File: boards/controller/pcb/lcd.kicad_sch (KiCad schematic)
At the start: 9 parts, among them J1001 Conn_01x15_Socket

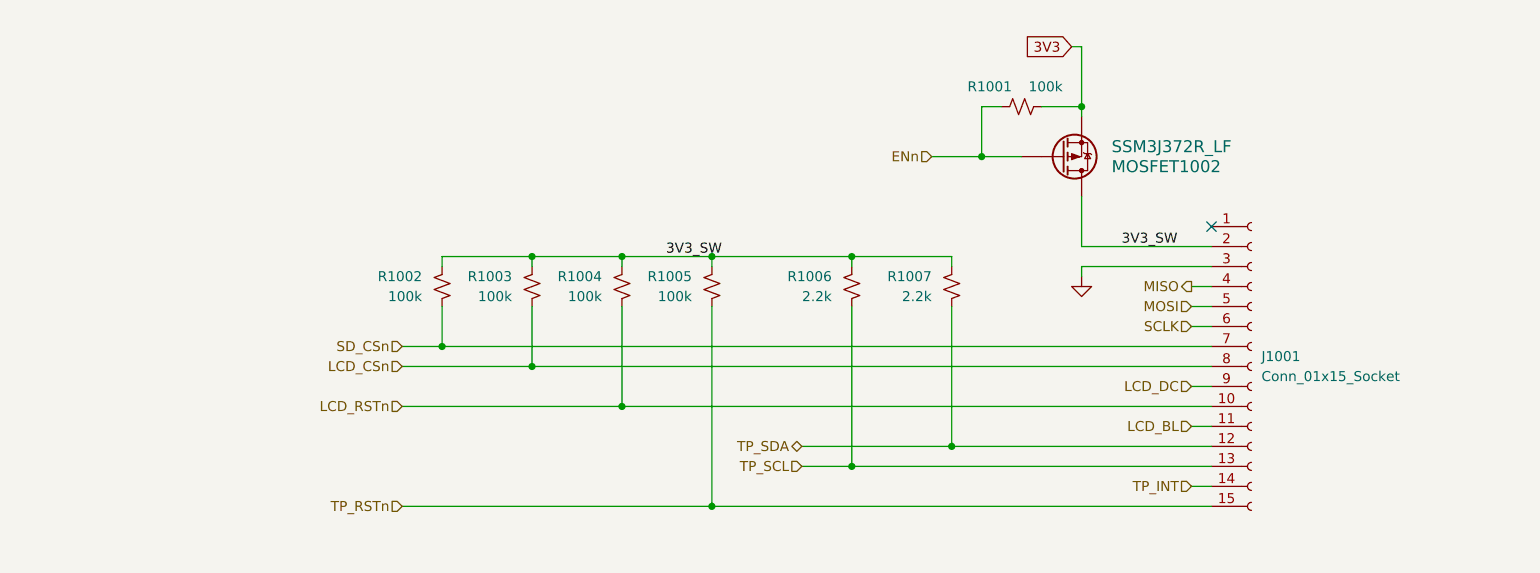
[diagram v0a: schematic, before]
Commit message: controller: pcb: Update schematic
Signed-off-by: Nicholas Loehrke <nicholasnloehrke@gmail.com>
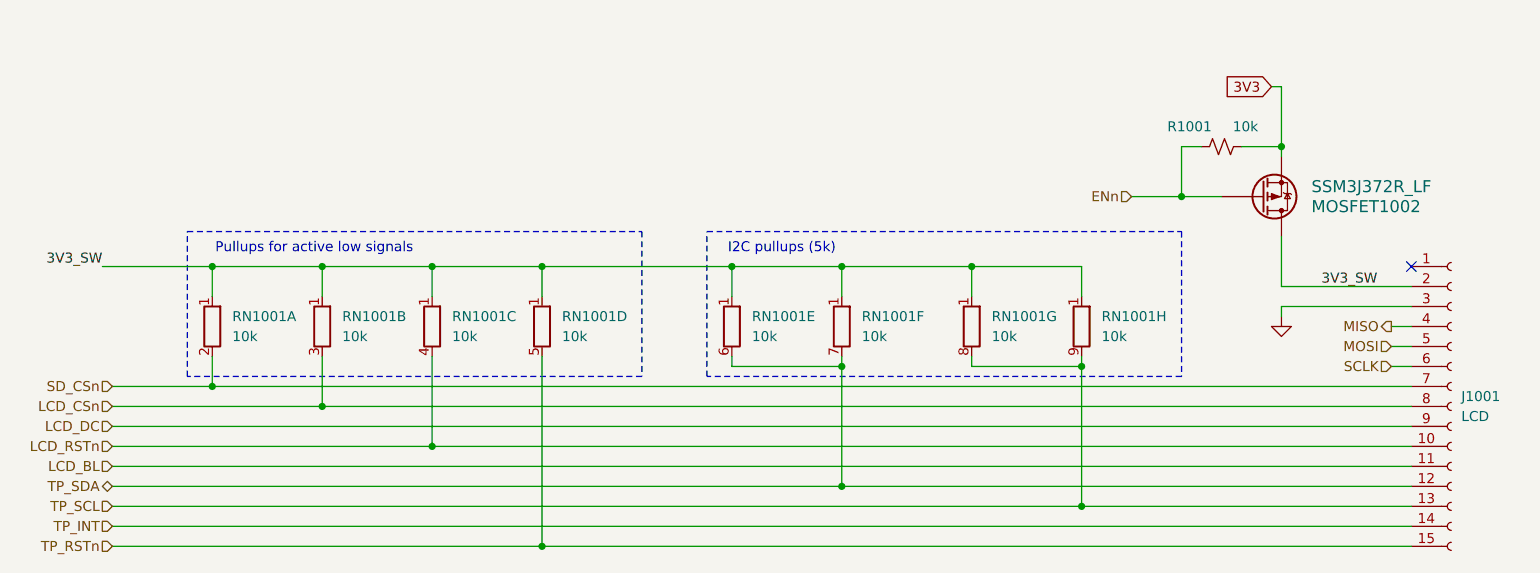
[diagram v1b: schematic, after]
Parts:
- removed R1002, R1003, R1004, R1005: 100k, symbol Device:R_Small_US
- removed R1006, R1007: 2.2k, symbol Device:R_Small_US
- added RN1001: 10k, Resistor_THT:R_Array_SIP9, symbol Device:R_Network08_Split
- J1001: value Conn_01x15_Socket -> LCD
- R1001: value 100k -> 10k
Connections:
- net 3V3_SW: now also RN1001.1 (R1), RN1001.1 (R1), RN1001.1 (R1), RN1001.1 (R1), RN1001.1 (R1), RN1001.1 (R1), RN1001.1 (R1), RN1001.1 (R1)
- net LCD_CSn: now also RN1001.3 (R2.2)
- net LCD_RSTn: now also RN1001.4 (R3.2)
- net SD_CSn: now also RN1001.2 (R1.2)
- net TP_RSTn: now also RN1001.5 (R4.2)
- net TP_SCL: now also RN1001.8 (R7.2), RN1001.9 (R8.2)
- net TP_SDA: now also RN1001.6 (R5.2), RN1001.7 (R6.2)
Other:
- note added: "I2C pullups (5k)"
- note added: "Pullups for active low signals"
- moved on the sheet: J1001, MOSFET1002, R1001

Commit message: controller: pcb: Update schematic
Signed-off-by: Nicholas Loehrke <nicholasnloehrke@gmail.com>
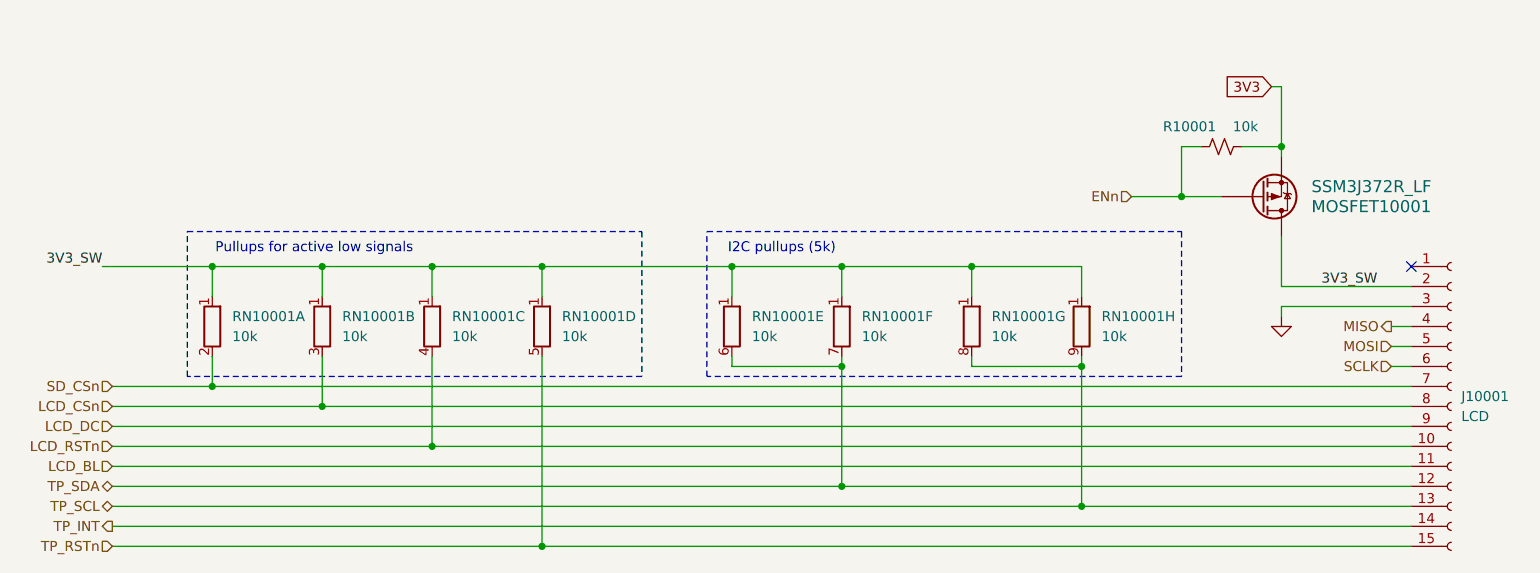
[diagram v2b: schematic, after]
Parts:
- renumbered J1001 to J10001, MOSFET1002 to MOSFET10001, R1001 to R10001, RN1001 to RN10001
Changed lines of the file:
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@@
 	)
 	(hierarchical_label "TP_SCL"
-		(shape input)
+		(shape bidirectional)
 		(at 60.96 119.38 180)
 		(effects
@@
 	)
 	(hierarchical_label "TP_INT"
-		(shape input)
+		(shape output)
 		(at 60.96 121.92 180)
 		(effects
@@
 		(dnp no)
 		(fields_autoplaced yes)
-		(property "Reference" "RN1001"
+		(property "Reference" "RN10001"
 			(at 156.21 95.2499 0)
 			(effects
@@
 			(project ""
 				(path "/5caba13a-97ae-46d4-856f-900b12012fd8/397b981f-9e39-4a0b-88ba-1021bd78e3f7"
-					(reference "RN1001")
+					(reference "RN10001")
 					(unit 6)
 				)
@@
 		(dnp no)
 		(fields_autoplaced yes)
-		(property "Reference" "RN1001"
+		(property "Reference" "RN10001"
 			(at 118.11 95.2499 0)
 			(effects
@@
 			(project ""
 				(path "/5caba13a-97ae-46d4-856f-900b12012fd8/397b981f-9e39-4a0b-88ba-1021bd78e3f7"
-					(reference "RN1001")
+					(reference "RN10001")
 					(unit 4)
 				)
@@
 		(dnp no)
 		(fields_autoplaced yes)
-		(property "Reference" "RN1001"
+		(property "Reference" "RN10001"
 			(at 142.24 95.2499 0)
 			(effects
@@
 			(project ""
 				(path "/5caba13a-97ae-46d4-856f-900b12012fd8/397b981f-9e39-4a0b-88ba-1021bd78e3f7"
-					(reference "RN1001")
+					(reference "RN10001")
 					(unit 5)
 				)
@@
 		(dnp no)
 		(fields_autoplaced yes)
-		(property "Reference" "RN1001"
+		(property "Reference" "RN10001"
 			(at 186.69 95.2499 0)
 			(effects
@@
 			(project ""
 				(path "/5caba13a-97ae-46d4-856f-900b12012fd8/397b981f-9e39-4a0b-88ba-1021bd78e3f7"
-					(reference "RN1001")
+					(reference "RN10001")
 					(unit 8)
 				)
@@
 		(dnp no)
 		(fields_autoplaced yes)
-		(property "Reference" "RN1001"
+		(property "Reference" "RN10001"
 			(at 104.14 95.2499 0)
 			(effects
@@
 			(project ""
 				(path "/5caba13a-97ae-46d4-856f-900b12012fd8/397b981f-9e39-4a0b-88ba-1021bd78e3f7"
-					(reference "RN1001")
+					(reference "RN10001")
 					(unit 3)
 				)
@@
 		(dnp no)
 		(fields_autoplaced yes)
-		(property "Reference" "#PWR01001"
+		(property "Reference" "#PWR010001"
 			(at 209.55 101.6 0)
 			(effects
@@
 			(project ""
 				(path "/5caba13a-97ae-46d4-856f-900b12012fd8/397b981f-9e39-4a0b-88ba-1021bd78e3f7"
-					(reference "#PWR01001")
+					(reference "#PWR010001")
 					(unit 1)
 				)
@@
 		(dnp no)
 		(fields_autoplaced yes)
-		(property "Reference" "RN1001"
+		(property "Reference" "RN10001"
 			(at 172.72 95.2499 0)
 			(effects
@@
 			(project ""
 				(path "/5caba13a-97ae-46d4-856f-900b12012fd8/397b981f-9e39-4a0b-88ba-1021bd78e3f7"
-					(reference "RN1001")
+					(reference "RN10001")
 					(unit 7)
 				)
@@
 		(dnp no)
 		(fields_autoplaced yes)
-		(property "Reference" "RN1001"
+		(property "Reference" "RN10001"
 			(at 76.2 95.2499 0)
 			(effects
@@
 			(project ""
 				(path "/5caba13a-97ae-46d4-856f-900b12012fd8/397b981f-9e39-4a0b-88ba-1021bd78e3f7"
-					(reference "RN1001")
+					(reference "RN10001")
 					(unit 1)
 				)
@@
 		(dnp no)
 		(fields_autoplaced yes)
-		(property "Reference" "RN1001"
+		(property "Reference" "RN10001"
 			(at 90.17 95.2499 0)
 			(effects
@@
 			(project ""
 				(path "/5caba13a-97ae-46d4-856f-900b12012fd8/397b981f-9e39-4a0b-88ba-1021bd78e3f7"
-					(reference "RN1001")
+					(reference "RN10001")
 					(unit 2)
 				)
@@
 		(dnp no)
 		(fields_autoplaced yes)
-		(property "Reference" "J1001"
+		(property "Reference" "J10001"
 			(at 232.41 105.4099 0)
 			(effects
@@
 			(project ""
 				(path "/5caba13a-97ae-46d4-856f-900b12012fd8/397b981f-9e39-4a0b-88ba-1021bd78e3f7"
-					(reference "J1001")
+					(reference "J10001")
 					(unit 1)
 				)
@@
 		(on_board yes)
 		(dnp no)
-		(property "Reference" "R1001"
+		(property "Reference" "R10001"
 			(at 197.866 71.12 90)
 			(effects
@@
 			(project ""
 				(path "/5caba13a-97ae-46d4-856f-900b12012fd8/397b981f-9e39-4a0b-88ba-1021bd78e3f7"
-					(reference "R1001")
+					(reference "R10001")
 					(unit 1)
 				)
@@
 		(on_board yes)
 		(dnp no)
-		(property "Reference" "MOSFET1002"
+		(property "Reference" "MOSFET10001"
 			(at 213.36 81.2801 0)
 			(effects
@@
 			(project ""
 				(path "/5caba13a-97ae-46d4-856f-900b12012fd8/397b981f-9e39-4a0b-88ba-1021bd78e3f7"
-					(reference "MOSFET1002")
+					(reference "MOSFET10001")
 					(unit 1)
 				)

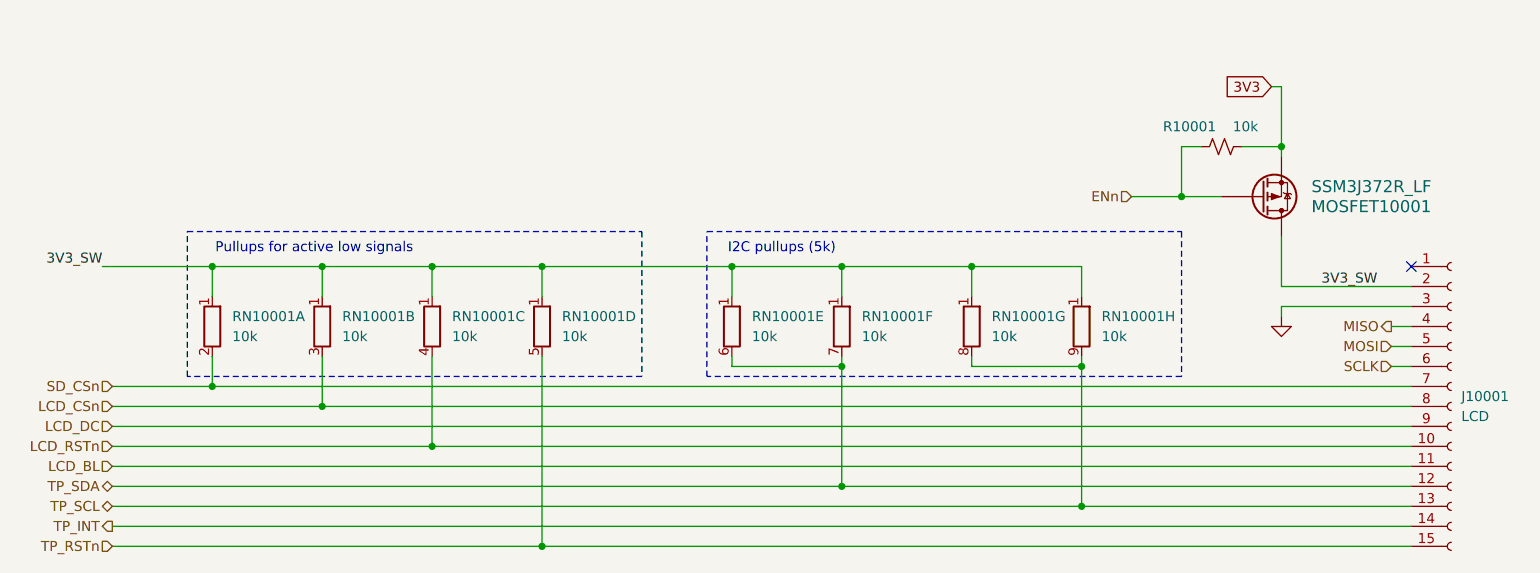
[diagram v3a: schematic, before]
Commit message: controller: pcb: Update schematic
Signed-off-by: Nicholas Loehrke <nicholasnloehrke@gmail.com>
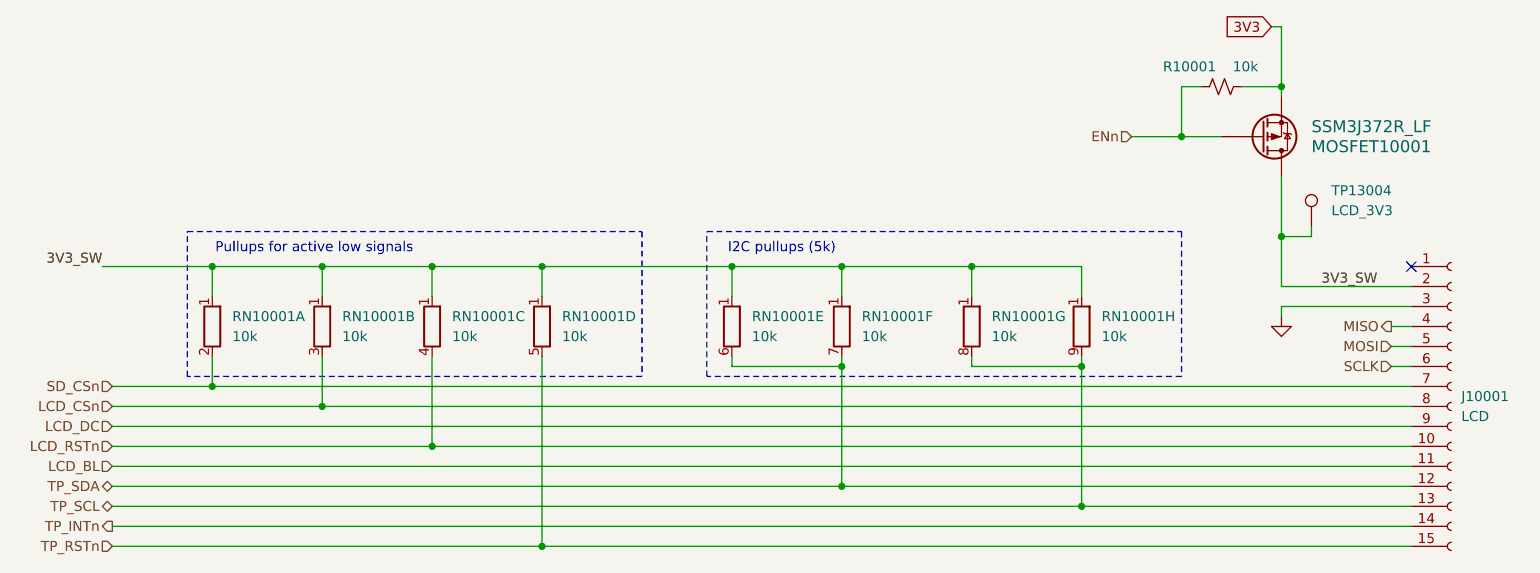
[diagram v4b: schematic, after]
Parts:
- added TP13004: LCD_3V3, symbol Connector:TestPoint
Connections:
- net 3V3_SW: now also TP13004.1
- net TP_INT renamed TP_INTn
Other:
- moved on the sheet: MOSFET10001, R10001
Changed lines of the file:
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@@
 	)
 	(junction
-		(at 196.85 80.01)
+		(at 196.85 72.39)
 		(diameter 0)
 		(color 0 0 0 0)
@@
 	)
 	(junction
+		(at 209.55 85.09)
+		(diameter 0)
+		(color 0 0 0 0)
+	)
+	(junction
 		(at 87.63 88.9)
 		(diameter 0)
@@
 	)
 	(junction
-		(at 209.55 73.66)
+		(at 209.55 66.04)
 		(diameter 0)
 		(color 0 0 0 0)
@@
 	(wire
 		(pts
-			(xy 204.47 73.66) (xy 209.55 73.66)
+			(xy 204.47 66.04) (xy 209.55 66.04)
 		)
 		(stroke
@@
 	(wire
 		(pts
+			(xy 213.36 83.82) (xy 213.36 85.09)
+		)
+		(stroke
+			(width 0)
+			(type default)
+		)
+	)
+	(wire
+		(pts
 			(xy 87.63 88.9) (xy 87.63 92.71)
 		)
@@
 	(wire
 		(pts
-			(xy 196.85 80.01) (xy 201.93 80.01)
-		)
-		(stroke
-			(width 0)
-			(type default)
-		)
-	)
-	(wire
-		(pts
-			(xy 209.55 73.66) (xy 209.55 74.93)
+			(xy 196.85 72.39) (xy 201.93 72.39)
+		)
+		(stroke
+			(width 0)
+			(type default)
+		)
+	)
+	(wire
+		(pts
+			(xy 209.55 66.04) (xy 209.55 67.31)
 		)
 		(stroke
@@
 	(wire
 		(pts
-			(xy 196.85 73.66) (xy 199.39 73.66)
+			(xy 196.85 66.04) (xy 199.39 66.04)
 		)
 		(stroke
@@
 	(wire
 		(pts
+			(xy 209.55 85.09) (xy 213.36 85.09)
+		)
+		(stroke
+			(width 0)
+			(type default)
+		)
+	)
+	(wire
+		(pts
 			(xy 101.6 88.9) (xy 115.57 88.9)
 		)
@@
 	(wire
 		(pts
-			(xy 209.55 66.04) (xy 209.55 73.66)
+			(xy 209.55 58.42) (xy 209.55 66.04)
 		)
 		(stroke
@@
 	(wire
 		(pts
-			(xy 196.85 73.66) (xy 196.85 80.01)
-		)
-		(stroke
-			(width 0)
-			(type default)
-		)
-	)
-	(wire
-		(pts
-			(xy 190.5 80.01) (xy 196.85 80.01)
+			(xy 196.85 66.04) (xy 196.85 72.39)
+		)
+		(stroke
+			(width 0)
+			(type default)
+		)
+	)
+	(wire
+		(pts
+			(xy 190.5 72.39) (xy 196.85 72.39)
 		)
 		(stroke
@@
 	(wire
 		(pts
+			(xy 209.55 85.09) (xy 209.55 77.47)
+		)
+		(stroke
+			(width 0.508)
+			(type default)
+		)
+	)
+	(wire
+		(pts
 			(xy 139.7 101.6) (xy 153.67 101.6)
 		)
@@
 	(wire
 		(pts
-			(xy 208.28 66.04) (xy 209.55 66.04)
+			(xy 208.28 58.42) (xy 209.55 58.42)
 		)
 		(stroke
@@
 	(global_label "3V3"
 		(shape input)
-		(at 208.28 66.04 180)
+		(at 208.28 58.42 180)
 		(fields_autoplaced yes)
 		(effects
@@
 		)
 		(property "Intersheetrefs" "${INTERSHEET_REFS}"
-			(at 201.7872 66.04 0)
+			(at 201.7872 58.42 0)
 			(effects
 				(font
@@
 		)
 	)
-	(hierarchical_label "TP_INT"
+	(hierarchical_label "TP_INTn"
 		(shape output)
 		(at 60.96 121.92 180)
@@
 	(hierarchical_label "ENn"
 		(shape input)
-		(at 190.5 80.01 180)
+		(at 190.5 72.39 180)
 		(effects
 			(font
@@
 	)
 	(symbol
+		(lib_id "Connector:TestPoint")
+		(at 213.36 83.82 0)
+		(unit 1)
+		(exclude_from_sim no)
+		(in_bom yes)
+		(on_board yes)
+		(dnp no)
+		(fields_autoplaced yes)
+		(property "Reference" "TP13004"
+			(at 215.9 79.2479 0)
+			(effects
+				(font
+					(size 1.27 1.27)
+				)
+				(justify left)
+			)
+		)
+		(property "Value" "LCD_3V3"
+			(at 215.9 81.7879 0)
+			(effects
+				(font
+					(size 1.27 1.27)
+				)
+				(justify left)
+			)
+		)
+		(property "Footprint" ""
+			(at 218.44 83.82 0)
+			(effects
+				(font
+					(size 1.27 1.27)
+				)
+				(hide yes)
+			)
+		)
+		(property "Datasheet" "~"
+			(at 218.44 83.82 0)
+			(effects
+				(font
+					(size 1.27 1.27)
+				)
+				(hide yes)
+			)
+		)
+		(property "Description" "test point"
+			(at 213.36 83.82 0)
+			(effects
+				(font
+					(size 1.27 1.27)
+				)
+				(hide yes)
+			)
+		)
+		(pin "1"
+		)
+		(instances
+			(project "controller"
+				(path "/5caba13a-97ae-46d4-856f-900b12012fd8/397b981f-9e39-4a0b-88ba-1021bd78e3f7"
+					(reference "TP13004")
+					(unit 1)
+				)
+			)
+		)
+	)
+	(symbol
 		(lib_id "Device:R_Network08_Split")
 		(at 139.7 96.52 0)
@@
 	(symbol
 		(lib_id "Device:R_Small_US")
-		(at 201.93 73.66 90)
+		(at 201.93 66.04 90)
 		(unit 1)
 		(exclude_from_sim no)
@@
 		(dnp no)
 		(property "Reference" "R10001"
-			(at 197.866 71.12 90)
+			(at 197.866 63.5 90)
 			(effects
 				(font
@@
 		)
 		(property "Value" "10k"
-			(at 204.978 71.12 90)
+			(at 204.978 63.5 90)
 			(effects
 				(font
@@
 		)
 		(property "Footprint" ""
-			(at 201.93 73.66 0)
+			(at 201.93 66.04 0)
 			(effects
 				(font
@@
 		)
 		(property "Datasheet" "~"
-			(at 201.93 73.66 0)
+			(at 201.93 66.04 0)
 			(effects
 				(font
@@
 		)
 		(property "Description" "Resistor, small US symbol"
-			(at 201.93 73.66 0)
+			(at 201.93 66.04 0)
 			(effects
 				(font
@@
 		(lib_name "SSM3J372R_LF_1")
 		(lib_id "SSM3J372R_LF:SSM3J372R_LF")
-		(at 201.93 80.01 0)
+		(at 201.93 72.39 0)
 		(mirror x)
 		(unit 1)
@@
 		(dnp no)
 		(property "Reference" "MOSFET10001"
-			(at 213.36 81.2801 0)
+			(at 213.36 73.6601 0)
 			(effects
 				(font
@@
 		)
 		(property "Value" "SSM3J372R_LF"
-			(at 213.36 78.7401 0)
+			(at 213.36 71.1201 0)
 			(effects
 				(font
@@
 		)
 		(property "Footprint" "SOT-23F_TOS"
-			(at 199.898 89.154 0)
+			(at 199.898 81.534 0)
 			(effects
 				(font
@@
 		)
 		(property "Datasheet" "SSM3J372R_LF"
-			(at 199.898 89.154 0)
+			(at 199.898 81.534 0)
 			(effects
 				(font
@@
 		)
 		(property "Description" ""
-			(at 201.93 80.01 0)
-			(effects
-				(font
+			(at 201.93 72.39 0)
+			(effects
+				(font
